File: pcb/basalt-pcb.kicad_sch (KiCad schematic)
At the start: 12 parts, among them J1 Conn_01x08_Pin, J2 Conn_01x08_Pin, J3 USB4215-03-A, J4 Conn_01x04_Pin, U1 DI78L3.3ZAB, U2 STM32C071F8Px

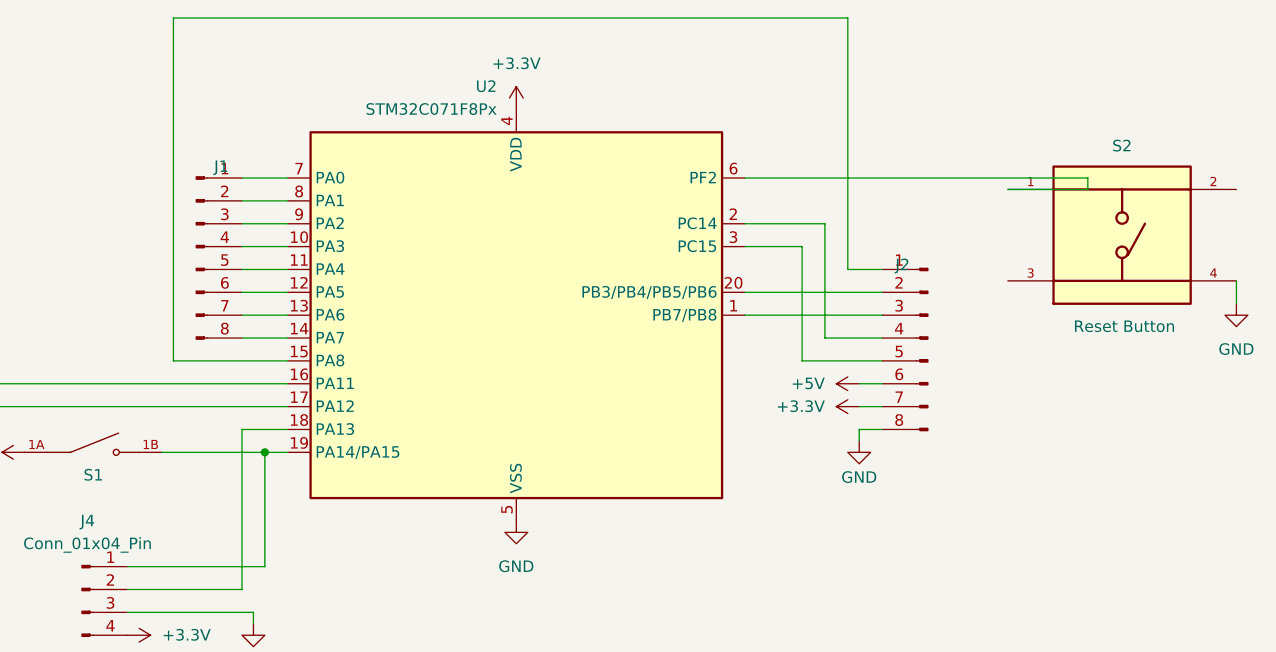
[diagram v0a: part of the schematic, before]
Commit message: Update with new pin count (removing pins that cannot be accessed with existing arduino ide variant), start work on arduino board config
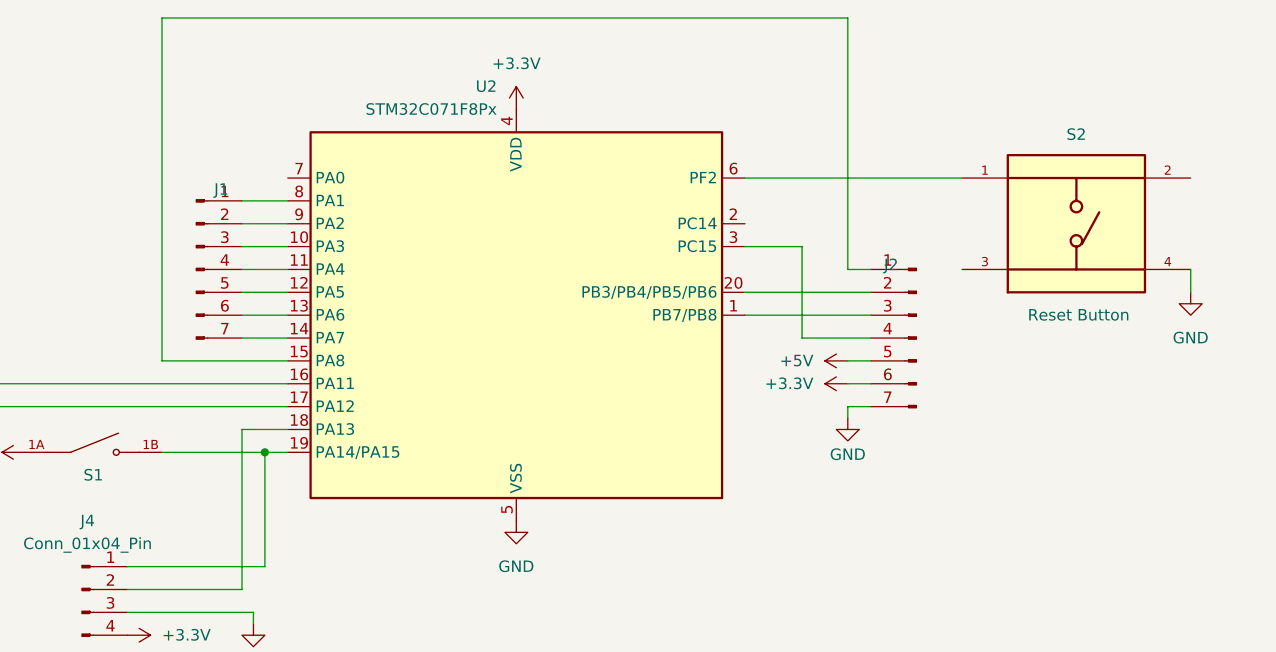
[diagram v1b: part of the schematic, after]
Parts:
- J1, J2: value Conn_01x08_Pin -> Conn_01x07_Pin; footprint Connector_PinHeader_2.54mm:PinHeader_1x08_P2.54mm_Vertical -> Connector_PinHeader_2.54mm:PinHeader_1x07_P2.54mm_Vertical; symbol Connector:Conn_01x08_Pin -> Connector:Conn_01x07_Pin
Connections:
- net +3.3V: now also J2.6 (Pin_6); no longer J2.7 (Pin_7)
- net +5V: now also J2.5 (Pin_5); no longer J2.6 (Pin_6)
- net GND: now also J2.7 (Pin_7); no longer J2.8 (Pin_8)
- net at J1.1 (Pin_1): now also U2.8 (PA1); no longer U2.7 (PA0)
- net at J1.2 (Pin_2): now also U2.9 (PA2); no longer U2.8 (PA1)
- net at J1.3 (Pin_3): now also U2.10 (PA3); no longer U2.9 (PA2)
- net at J1.4 (Pin_4): now also U2.11 (PA4); no longer U2.10 (PA3)
- net at J1.5 (Pin_5): now also U2.12 (PA5); no longer U2.11 (PA4)
- net at J1.6 (Pin_6): now also U2.13 (PA6); no longer U2.12 (PA5)
- net at J1.7 (Pin_7): now also U2.14 (PA7); no longer U2.13 (PA6)
- net at J2.4 (Pin_4): now also U2.3 (PC15); no longer U2.2 (PC14)
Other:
- moved on the sheet: S2

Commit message: Switch to using STM32C071G8U6 that is supported by STM32duino currently
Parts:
- U2: footprint Package_SO:TSSOP-20_4.4x6.5mm_P0.65mm -> Package_DFN_QFN:QFN-28_4x4mm_P0.5mm; symbol MCU_ST_STM32C0:STM32C071F8Px -> MCU_ST_STM32C0:STM32C071G8Ux
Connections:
- net +3.3V: now also U2.3 (VDD); no longer U2.4 (VDD)
- net GND: now also U2.4 (VSS); no longer U2.5 (VSS)
- net at J1.1 (Pin_1): now also U2.6 (PA0); no longer U2.8 (PA1)
- net at J1.2 (Pin_2): now also U2.7 (PA1); no longer U2.9 (PA2)
- net at J1.3 (Pin_3): now also U2.8 (PA2); no longer U2.10 (PA3)
- net at J1.4 (Pin_4): now also U2.9 (PA3); no longer U2.11 (PA4)
- net at J1.5 (Pin_5): now also U2.10 (PA4); no longer U2.12 (PA5)
- net at J1.6 (Pin_6): now also U2.11 (PA5); no longer U2.13 (PA6)
- net at J1.7 (Pin_7): now also U2.12 (PA6); no longer U2.14 (PA7)
- net at J3.A6 (DP1), J3.B6 (DP2): now also U2.19 (PA12); no longer U2.17 (PA12)
- net at J3.A7 (DN1), J3.B7 (DN2): now also U2.18 (PA11); no longer U2.16 (PA11)
- net at J2.1 (Pin_1): now also U2.13 (PA7); no longer U2.15 (PA8)
- net at J2.2 (Pin_2): now also U2.16 (PA8); no longer U2.20 (PB3/PB4/PB5/PB6)
- net at J2.4 (Pin_4): now also U2.2 (PC15); no longer U2.3 (PC15)
- net at J4.1 (Pin_1), S1.1B: now also U2.21 (PA14); no longer U2.19 (PA14/PA15)
- net at J4.2 (Pin_2): now also U2.20 (PA13); no longer U2.18 (PA13)
- net at S2.1: now also U2.5 (PF2); no longer U2.6 (PF2)
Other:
- moved on the sheet: J1
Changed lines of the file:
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@@
 	(wire
 		(pts
-			(xy 190.5 74.93) (xy 190.5 85.09)
-		)
-		(stroke
-			(width 0)
-			(type default)
-		)
-	)
-	(wire
-		(pts
-			(xy 128.27 74.93) (xy 133.35 74.93)
+			(xy 128.27 72.39) (xy 148.59 72.39)
 		)
 		(stroke
@@
 	(wire
 		(pts
-			(xy 184.15 80.01) (xy 198.12 80.01)
-		)
-		(stroke
-			(width 0)
-			(type default)
-		)
-	)
-	(wire
-		(pts
 			(xy 77.47 80.01) (xy 77.47 77.47)
 		)
@@
 	(wire
 		(pts
-			(xy 130.81 97.79) (xy 133.35 97.79)
+			(xy 130.81 97.79) (xy 148.59 97.79)
 		)
 		(stroke
@@
 	(wire
 		(pts
+			(xy 190.5 82.55) (xy 198.12 82.55)
+		)
+		(stroke
+			(width 0)
+			(type default)
+		)
+	)
+	(wire
+		(pts
+			(xy 193.04 80.01) (xy 198.12 80.01)
+		)
+		(stroke
+			(width 0)
+			(type default)
+		)
+	)
+	(wire
+		(pts
 			(xy 80.01 97.79) (xy 77.47 97.79)
 		)
@@
 	(wire
 		(pts
-			(xy 184.15 74.93) (xy 190.5 74.93)
+			(xy 187.96 85.09) (xy 198.12 85.09)
 		)
 		(stroke
@@
 	(wire
 		(pts
-			(xy 128.27 77.47) (xy 133.35 77.47)
+			(xy 128.27 74.93) (xy 148.59 74.93)
 		)
 		(stroke
@@
 	(wire
 		(pts
+			(xy 168.91 67.31) (xy 208.28 67.31)
+		)
+		(stroke
+			(width 0)
+			(type default)
+		)
+	)
+	(wire
+		(pts
 			(xy 198.12 87.63) (xy 195.58 87.63)
 		)
@@
 	(wire
 		(pts
-			(xy 184.15 82.55) (xy 198.12 82.55)
-		)
-		(stroke
-			(width 0)
-			(type default)
-		)
-	)
-	(wire
-		(pts
 			(xy 233.68 80.01) (xy 233.68 77.47)
 		)
@@
 	(wire
 		(pts
+			(xy 148.59 87.63) (xy 116.84 87.63)
+		)
+		(stroke
+			(width 0)
+			(type default)
+		)
+	)
+	(wire
+		(pts
+			(xy 190.5 74.93) (xy 190.5 82.55)
+		)
+		(stroke
+			(width 0)
+			(type default)
+		)
+	)
+	(wire
+		(pts
 			(xy 119.38 97.79) (xy 130.81 97.79)
 		)
@@
 	(wire
 		(pts
-			(xy 128.27 80.01) (xy 133.35 80.01)
+			(xy 128.27 77.47) (xy 148.59 77.47)
 		)
 		(stroke
@@
 	(wire
 		(pts
-			(xy 184.15 67.31) (xy 208.28 67.31)
+			(xy 168.91 77.47) (xy 187.96 77.47)
 		)
 		(stroke
@@
 	(wire
 		(pts
-			(xy 82.55 90.17) (xy 133.35 90.17)
-		)
-		(stroke
-			(width 0)
-			(type default)
-		)
-	)
-	(wire
-		(pts
-			(xy 190.5 85.09) (xy 198.12 85.09)
+			(xy 82.55 90.17) (xy 148.59 90.17)
 		)
 		(stroke
@@
 	(wire
 		(pts
-			(xy 80.01 92.71) (xy 133.35 92.71)
+			(xy 80.01 92.71) (xy 148.59 92.71)
+		)
+		(stroke
+			(width 0)
+			(type default)
+		)
+	)
+	(wire
+		(pts
+			(xy 193.04 52.07) (xy 193.04 80.01)
 		)
 		(stroke
@@
 	(wire
 		(pts
-			(xy 119.38 87.63) (xy 133.35 87.63)
+			(xy 119.38 85.09) (xy 148.59 85.09)
 		)
 		(stroke
@@
 	(wire
 		(pts
+			(xy 116.84 52.07) (xy 193.04 52.07)
+		)
+		(stroke
+			(width 0)
+			(type default)
+		)
+	)
+	(wire
+		(pts
 			(xy 198.12 92.71) (xy 195.58 92.71)
 		)
@@
 	(wire
 		(pts
-			(xy 133.35 95.25) (xy 128.27 95.25)
+			(xy 128.27 95.25) (xy 148.59 95.25)
 		)
 		(stroke
@@
 	(wire
 		(pts
-			(xy 128.27 72.39) (xy 133.35 72.39)
-		)
-		(stroke
-			(width 0)
-			(type default)
-		)
-	)
-	(wire
-		(pts
-			(xy 119.38 49.53) (xy 119.38 87.63)
-		)
-		(stroke
-			(width 0)
-			(type default)
-		)
-	)
-	(wire
-		(pts
-			(xy 128.27 85.09) (xy 133.35 85.09)
-		)
-		(stroke
-			(width 0)
-			(type default)
-		)
-	)
-	(wire
-		(pts
-			(xy 128.27 69.85) (xy 133.35 69.85)
+			(xy 128.27 69.85) (xy 148.59 69.85)
+		)
+		(stroke
+			(width 0)
+			(type default)
+		)
+	)
+	(wire
+		(pts
+			(xy 119.38 49.53) (xy 119.38 85.09)
+		)
+		(stroke
+			(width 0)
+			(type default)
+		)
+	)
+	(wire
+		(pts
+			(xy 187.96 77.47) (xy 187.96 85.09)
+		)
+		(stroke
+			(width 0)
+			(type default)
+		)
+	)
+	(wire
+		(pts
+			(xy 168.91 74.93) (xy 190.5 74.93)
+		)
+		(stroke
+			(width 0)
+			(type default)
+		)
+	)
+	(wire
+		(pts
+			(xy 128.27 82.55) (xy 148.59 82.55)
+		)
+		(stroke
+			(width 0)
+			(type default)
+		)
+	)
+	(wire
+		(pts
+			(xy 128.27 67.31) (xy 148.59 67.31)
 		)
 		(stroke
@@
 	(wire
 		(pts
-			(xy 128.27 82.55) (xy 133.35 82.55)
+			(xy 128.27 80.01) (xy 148.59 80.01)
 		)
 		(stroke
@@
 		(pts
 			(xy 129.54 115.57) (xy 129.54 116.84)
+		)
+		(stroke
+			(width 0)
+			(type default)
+		)
+	)
+	(wire
+		(pts
+			(xy 116.84 87.63) (xy 116.84 52.07)
 		)
 		(stroke
@@
 	(symbol
 		(lib_id "Connector:Conn_01x07_Pin")
-		(at 123.19 77.47 0)
+		(at 123.19 74.93 0)
 		(unit 1)
 		(body_style 1)
@@
 		(dnp no)
 		(property "Reference" "J1"
-			(at 125.984 68.58 0)
+			(at 125.984 66.04 0)
 			(show_name no)
 			(do_not_autoplace no)
@@
 		)
 		(property "Value" "Conn_01x07_Pin"
-			(at 123.825 69.85 0)
+			(at 123.825 67.31 0)
 			(hide yes)
 			(show_name no)
@@
 		)
 		(property "Footprint" "Connector_PinHeader_2.54mm:PinHeader_1x07_P2.54mm_Vertical"
-			(at 123.19 77.47 0)
+			(at 123.19 74.93 0)
 			(hide yes)
 			(show_name no)
@@
 		)
 		(property "Datasheet" ""
-			(at 123.19 77.47 0)
+			(at 123.19 74.93 0)
 			(hide yes)
 			(show_name no)
@@
 		)
 		(property "Description" "Generic connector, single row, 01x07, script generated"
-			(at 123.19 77.47 0)
+			(at 123.19 74.93 0)
 			(hide yes)
 			(show_name no)
@@
 	(symbol
 		(lib_id "power:GND")
-		(at 158.75 105.41 0)
+		(at 158.75 107.95 0)
 		(unit 1)
 		(body_style 1)
@@
 		(dnp no)
 		(property "Reference" "#PWR02"
-			(at 158.75 111.76 0)
+			(at 158.75 114.3 0)
 			(hide yes)
 			(show_name no)
@@
 		)
 		(property "Value" "GND"
-			(at 158.75 110.49 0)
+			(at 158.75 113.03 0)
 			(show_name no)
 			(do_not_autoplace no)
@@
 		)
 		(property "Footprint" ""
-			(at 158.75 105.41 0)
+			(at 158.75 107.95 0)
 			(hide yes)
 			(show_name no)
@@
 		)
 		(property "Datasheet" ""
-			(at 158.75 105.41 0)
+			(at 158.75 107.95 0)
 			(hide yes)
 			(show_name no)
@@
 		)
 		(property "Description" "Power symbol creates a global label with name \"GND\" , ground"
-			(at 158.75 105.41 0)
+			(at 158.75 107.95 0)
 			(hide yes)
 			(show_name no)
@@
 	)
 	(symbol
-		(lib_id "MCU_ST_STM32C0:STM32C071F8Px")
-		(at 158.75 82.55 0)
+		(lib_id "MCU_ST_STM32C0:STM32C071G8Ux")
+		(at 158.75 85.09 0)
 		(mirror y)
 		(unit 1)
@@
 		(dnp no)
 		(property "Reference" "U2"
-			(at 156.6067 57.15 0)
+			(at 156.6067 59.69 0)
 			(show_name no)
 			(do_not_autoplace no)
@@
 		)
 		(property "Value" "STM32C071F8Px"
-			(at 156.6067 59.69 0)
+			(at 156.6067 62.23 0)
 			(show_name no)
 			(do_not_autoplace no)
@@
 			)
 		)
-		(property "Footprint" "Package_SO:TSSOP-20_4.4x6.5mm_P0.65mm"
-			(at 181.61 102.87 0)
+		(property "Footprint" "Package_DFN_QFN:QFN-28_4x4mm_P0.5mm"
+			(at 166.37 105.41 0)
 			(hide yes)
 			(show_name no)
@@
 			)
 		)
-		(property "Datasheet" "https://www.st.com/resource/en/datasheet/stm32c071f8.pdf"
-			(at 158.75 82.55 0)
-			(hide yes)
-			(show_name no)
-			(do_not_autoplace no)
-			(effects
-				(font
-					(size 1.27 1.27)
-				)
-			)
-		)
-		(property "Description" "STMicroelectronics Arm Cortex-M0+ MCU, 64KB flash, 24KB RAM, 18 GPIO, TSSOP20_GP"
-			(at 158.75 82.55 0)
+		(property "Datasheet" "https://www.st.com/resource/en/datasheet/stm32c071g8.pdf"
+			(at 158.75 85.09 0)
+			(hide yes)
+			(show_name no)
+			(do_not_autoplace no)
+			(effects
+				(font
+					(size 1.27 1.27)
+				)
+			)
+		)
+		(property "Description" "STMicroelectronics Arm Cortex-M0+ MCU, 64KB flash, 24KB RAM, 26 GPIO, UFQFPN28_GP"
+			(at 158.75 85.09 0)
 			(hide yes)
 			(show_name no)
@@
 		(pin "1"
 		)
+		(pin "28"
+		)
+		(pin "26"
+		)
+		(pin "27"
+		)
+		(pin "23"
+		)
+		(pin "21"
+		)
+		(pin "25"
+		)
+		(pin "22"
+		)
+		(pin "24"
+		)
 		(instances

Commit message: Undo accidental merge...
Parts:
- U2: footprint Package_DFN_QFN:QFN-28_4x4mm_P0.5mm -> Package_SO:TSSOP-20_4.4x6.5mm_P0.65mm; symbol MCU_ST_STM32C0:STM32C071G8Ux -> MCU_ST_STM32C0:STM32C071F8Px
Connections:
- net +3.3V: now also U2.4 (VDD); no longer U2.3 (VDD)
- net GND: now also U2.5 (VSS); no longer U2.4 (VSS)
- net at J1.1 (Pin_1): now also U2.8 (PA1); no longer U2.6 (PA0)
- net at J1.2 (Pin_2): now also U2.9 (PA2); no longer U2.7 (PA1)
- net at J1.3 (Pin_3): now also U2.10 (PA3); no longer U2.8 (PA2)
- net at J1.4 (Pin_4): now also U2.11 (PA4); no longer U2.9 (PA3)
- net at J1.5 (Pin_5): now also U2.12 (PA5); no longer U2.10 (PA4)
- net at J1.6 (Pin_6): now also U2.13 (PA6); no longer U2.11 (PA5)
- net at J1.7 (Pin_7): now also U2.14 (PA7); no longer U2.12 (PA6)
- net at J3.A6 (DP1), J3.B6 (DP2): now also U2.17 (PA12); no longer U2.19 (PA12)
- net at J3.A7 (DN1), J3.B7 (DN2): now also U2.16 (PA11); no longer U2.18 (PA11)
- net at J2.1 (Pin_1): now also U2.15 (PA8); no longer U2.13 (PA7)
- net at J2.2 (Pin_2): now also U2.20 (PB3/PB4/PB5/PB6); no longer U2.16 (PA8)
- net at J2.4 (Pin_4): now also U2.3 (PC15); no longer U2.2 (PC15)
- net at J4.1 (Pin_1), S1.1B: now also U2.19 (PA14/PA15); no longer U2.21 (PA14)
- net at J4.2 (Pin_2): now also U2.18 (PA13); no longer U2.20 (PA13)
- net at S2.1: now also U2.6 (PF2); no longer U2.5 (PF2)
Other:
- moved on the sheet: J1
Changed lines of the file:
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@@
 	(wire
 		(pts
-			(xy 128.27 72.39) (xy 148.59 72.39)
+			(xy 190.5 74.93) (xy 190.5 85.09)
+		)
+		(stroke
+			(width 0)
+			(type default)
+		)
+	)
+	(wire
+		(pts
+			(xy 128.27 74.93) (xy 133.35 74.93)
 		)
 		(stroke
@@
 	(wire
 		(pts
+			(xy 184.15 80.01) (xy 198.12 80.01)
+		)
+		(stroke
+			(width 0)
+			(type default)
+		)
+	)
+	(wire
+		(pts
 			(xy 77.47 80.01) (xy 77.47 77.47)
 		)
@@
 	(wire
 		(pts
-			(xy 130.81 97.79) (xy 148.59 97.79)
+			(xy 130.81 97.79) (xy 133.35 97.79)
 		)
 		(stroke
@@
 	(wire
 		(pts
-			(xy 190.5 82.55) (xy 198.12 82.55)
-		)
-		(stroke
-			(width 0)
-			(type default)
-		)
-	)
-	(wire
-		(pts
-			(xy 193.04 80.01) (xy 198.12 80.01)
-		)
-		(stroke
-			(width 0)
-			(type default)
-		)
-	)
-	(wire
-		(pts
 			(xy 80.01 97.79) (xy 77.47 97.79)
 		)
@@
 	(wire
 		(pts
-			(xy 187.96 85.09) (xy 198.12 85.09)
+			(xy 184.15 74.93) (xy 190.5 74.93)
 		)
 		(stroke
@@
 	(wire
 		(pts
-			(xy 128.27 74.93) (xy 148.59 74.93)
+			(xy 128.27 77.47) (xy 133.35 77.47)
 		)
 		(stroke
@@
 	(wire
 		(pts
-			(xy 168.91 67.31) (xy 208.28 67.31)
-		)
-		(stroke
-			(width 0)
-			(type default)
-		)
-	)
-	(wire
-		(pts
 			(xy 198.12 87.63) (xy 195.58 87.63)
 		)
@@
 	(wire
 		(pts
+			(xy 184.15 82.55) (xy 198.12 82.55)
+		)
+		(stroke
+			(width 0)
+			(type default)
+		)
+	)
+	(wire
+		(pts
 			(xy 233.68 80.01) (xy 233.68 77.47)
 		)
@@
 	(wire
 		(pts
-			(xy 148.59 87.63) (xy 116.84 87.63)
-		)
-		(stroke
-			(width 0)
-			(type default)
-		)
-	)
-	(wire
-		(pts
-			(xy 190.5 74.93) (xy 190.5 82.55)
-		)
-		(stroke
-			(width 0)
-			(type default)
-		)
-	)
-	(wire
-		(pts
 			(xy 119.38 97.79) (xy 130.81 97.79)
 		)
@@
 	(wire
 		(pts
-			(xy 128.27 77.47) (xy 148.59 77.47)
+			(xy 128.27 80.01) (xy 133.35 80.01)
 		)
 		(stroke
@@
 	(wire
 		(pts
-			(xy 168.91 77.47) (xy 187.96 77.47)
+			(xy 184.15 67.31) (xy 208.28 67.31)
 		)
 		(stroke
@@
 	(wire
 		(pts
-			(xy 82.55 90.17) (xy 148.59 90.17)
+			(xy 82.55 90.17) (xy 133.35 90.17)
+		)
+		(stroke
+			(width 0)
+			(type default)
+		)
+	)
+	(wire
+		(pts
+			(xy 190.5 85.09) (xy 198.12 85.09)
 		)
 		(stroke
@@
 	(wire
 		(pts
-			(xy 80.01 92.71) (xy 148.59 92.71)
-		)
-		(stroke
-			(width 0)
-			(type default)
-		)
-	)
-	(wire
-		(pts
-			(xy 193.04 52.07) (xy 193.04 80.01)
+			(xy 80.01 92.71) (xy 133.35 92.71)
 		)
 		(stroke
@@
 	(wire
 		(pts
-			(xy 119.38 85.09) (xy 148.59 85.09)
+			(xy 119.38 87.63) (xy 133.35 87.63)
 		)
 		(stroke
@@
 	(wire
 		(pts
-			(xy 116.84 52.07) (xy 193.04 52.07)
-		)
-		(stroke
-			(width 0)
-			(type default)
-		)
-	)
-	(wire
-		(pts
 			(xy 198.12 92.71) (xy 195.58 92.71)
 		)
@@
 	(wire
 		(pts
-			(xy 128.27 95.25) (xy 148.59 95.25)
+			(xy 133.35 95.25) (xy 128.27 95.25)
 		)
 		(stroke
@@
 	(wire
 		(pts
-			(xy 128.27 69.85) (xy 148.59 69.85)
-		)
-		(stroke
-			(width 0)
-			(type default)
-		)
-	)
-	(wire
-		(pts
-			(xy 119.38 49.53) (xy 119.38 85.09)
-		)
-		(stroke
-			(width 0)
-			(type default)
-		)
-	)
-	(wire
-		(pts
-			(xy 187.96 77.47) (xy 187.96 85.09)
-		)
-		(stroke
-			(width 0)
-			(type default)
-		)
-	)
-	(wire
-		(pts
-			(xy 168.91 74.93) (xy 190.5 74.93)
-		)
-		(stroke
-			(width 0)
-			(type default)
-		)
-	)
-	(wire
-		(pts
-			(xy 128.27 82.55) (xy 148.59 82.55)
-		)
-		(stroke
-			(width 0)
-			(type default)
-		)
-	)
-	(wire
-		(pts
-			(xy 128.27 67.31) (xy 148.59 67.31)
+			(xy 128.27 72.39) (xy 133.35 72.39)
+		)
+		(stroke
+			(width 0)
+			(type default)
+		)
+	)
+	(wire
+		(pts
+			(xy 119.38 49.53) (xy 119.38 87.63)
+		)
+		(stroke
+			(width 0)
+			(type default)
+		)
+	)
+	(wire
+		(pts
+			(xy 128.27 85.09) (xy 133.35 85.09)
+		)
+		(stroke
+			(width 0)
+			(type default)
+		)
+	)
+	(wire
+		(pts
+			(xy 128.27 69.85) (xy 133.35 69.85)
 		)
 		(stroke
@@
 	(wire
 		(pts
-			(xy 128.27 80.01) (xy 148.59 80.01)
+			(xy 128.27 82.55) (xy 133.35 82.55)
 		)
 		(stroke
@@
 		(pts
 			(xy 129.54 115.57) (xy 129.54 116.84)
-		)
-		(stroke
-			(width 0)
-			(type default)
-		)
-	)
-	(wire
-		(pts
-			(xy 116.84 87.63) (xy 116.84 52.07)
 		)
 		(stroke
@@
 	(symbol
 		(lib_id "Connector:Conn_01x07_Pin")
-		(at 123.19 74.93 0)
+		(at 123.19 77.47 0)
 		(unit 1)
 		(body_style 1)
@@
 		(dnp no)
 		(property "Reference" "J1"
-			(at 125.984 66.04 0)
+			(at 125.984 68.58 0)
 			(show_name no)
 			(do_not_autoplace no)
@@
 		)
 		(property "Value" "Conn_01x07_Pin"
-			(at 123.825 67.31 0)
+			(at 123.825 69.85 0)
 			(hide yes)
 			(show_name no)
@@
 		)
 		(property "Footprint" "Connector_PinHeader_2.54mm:PinHeader_1x07_P2.54mm_Vertical"
-			(at 123.19 74.93 0)
+			(at 123.19 77.47 0)
 			(hide yes)
 			(show_name no)
@@
 		)
 		(property "Datasheet" ""
-			(at 123.19 74.93 0)
+			(at 123.19 77.47 0)
 			(hide yes)
 			(show_name no)
@@
 		)
 		(property "Description" "Generic connector, single row, 01x07, script generated"
-			(at 123.19 74.93 0)
+			(at 123.19 77.47 0)
 			(hide yes)
 			(show_name no)
@@
 	(symbol
 		(lib_id "power:GND")
-		(at 158.75 107.95 0)
+		(at 158.75 105.41 0)
 		(unit 1)
 		(body_style 1)
@@
 		(dnp no)
 		(property "Reference" "#PWR02"
-			(at 158.75 114.3 0)
+			(at 158.75 111.76 0)
 			(hide yes)
 			(show_name no)
@@
 		)
 		(property "Value" "GND"
-			(at 158.75 113.03 0)
+			(at 158.75 110.49 0)
 			(show_name no)
 			(do_not_autoplace no)
@@
 		)
 		(property "Footprint" ""
-			(at 158.75 107.95 0)
+			(at 158.75 105.41 0)
 			(hide yes)
 			(show_name no)
@@
 		)
 		(property "Datasheet" ""
-			(at 158.75 107.95 0)
+			(at 158.75 105.41 0)
 			(hide yes)
 			(show_name no)
@@
 		)
 		(property "Description" "Power symbol creates a global label with name \"GND\" , ground"
-			(at 158.75 107.95 0)
+			(at 158.75 105.41 0)
 			(hide yes)
 			(show_name no)
@@
 	)
 	(symbol
-		(lib_id "MCU_ST_STM32C0:STM32C071G8Ux")
-		(at 158.75 85.09 0)
+		(lib_id "MCU_ST_STM32C0:STM32C071F8Px")
+		(at 158.75 82.55 0)
 		(mirror y)
 		(unit 1)
@@
 		(dnp no)
 		(property "Reference" "U2"
+			(at 156.6067 57.15 0)
+			(show_name no)
+			(do_not_autoplace no)
+			(effects
+				(font
+					(size 1.27 1.27)
+				)
+				(justify left)
+			)
+		)
+		(property "Value" "STM32C071F8Px"
 			(at 156.6067 59.69 0)
 			(show_name no)
@@
 			)
 		)
-		(property "Value" "STM32C071F8Px"
-			(at 156.6067 62.23 0)
-			(show_name no)
-			(do_not_autoplace no)
-			(effects
-				(font
-					(size 1.27 1.27)
-				)
-				(justify left)
-			)
-		)
-		(property "Footprint" "Package_DFN_QFN:QFN-28_4x4mm_P0.5mm"
-			(at 166.37 105.41 0)
+		(property "Footprint" "Package_SO:TSSOP-20_4.4x6.5mm_P0.65mm"
+			(at 181.61 102.87 0)
 			(hide yes)
 			(show_name no)
@@
 			)
 		)
-		(property "Datasheet" "https://www.st.com/resource/en/datasheet/stm32c071g8.pdf"
-			(at 158.75 85.09 0)
-			(hide yes)
-			(show_name no)
-			(do_not_autoplace no)
-			(effects
-				(font
-					(size 1.27 1.27)
-				)
-			)
-		)
-		(property "Description" "STMicroelectronics Arm Cortex-M0+ MCU, 64KB flash, 24KB RAM, 26 GPIO, UFQFPN28_GP"
-			(at 158.75 85.09 0)
+		(property "Datasheet" "https://www.st.com/resource/en/datasheet/stm32c071f8.pdf"
+			(at 158.75 82.55 0)
+			(hide yes)
+			(show_name no)
+			(do_not_autoplace no)
+			(effects
+				(font
+					(size 1.27 1.27)
+				)
+			)
+		)
+		(property "Description" "STMicroelectronics Arm Cortex-M0+ MCU, 64KB flash, 24KB RAM, 18 GPIO, TSSOP20_GP"
+			(at 158.75 82.55 0)
 			(hide yes)
 			(show_name no)
@@
 		(pin "1"
 		)
-		(pin "28"
-		)
-		(pin "26"
-		)
-		(pin "27"
-		)
-		(pin "23"
-		)
-		(pin "21"
-		)
-		(pin "25"
-		)
-		(pin "22"
-		)
-		(pin "24"
-		)
 		(instances

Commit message: Minor updates to pcb, update gitignore
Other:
- company: (none) -> OC ECE MESA
- title: (none) -> MESA Basalt
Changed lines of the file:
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@@
 	(generator_version "10.0")
 	(paper "A4")
+	(title_block
+		(title "MESA Basalt")
+		(date "2026-05-02")
+		(rev "2")
+		(company "OC ECE MESA")
+	)
 	(junction
 		(at 85.09 82.55)

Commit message: Fix mounting holes
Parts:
- added H1, H2, H3, H4: MountingHole_Pad, MountingHole:MountingHole_2.2mm_M2_Pad, symbol Mechanical:MountingHole_Pad
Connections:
- net GND: now also H1.1, H2.1, H3.1, H4.1
